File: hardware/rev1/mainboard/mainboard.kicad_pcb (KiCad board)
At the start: 2 copper layers, 40 x 108 mm, 60 parts, among them J1 CONN_05X2SHD, J2 Conn_01x10_Female, J3 Conn_01x10_Female, U1 LM1117-5.0, U2 TPS79633, U3 SAMD51J, U4 OPA388, U5 W25Q32FVSS, U6 AD5685xRUZ, U7 SN74AHCT125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

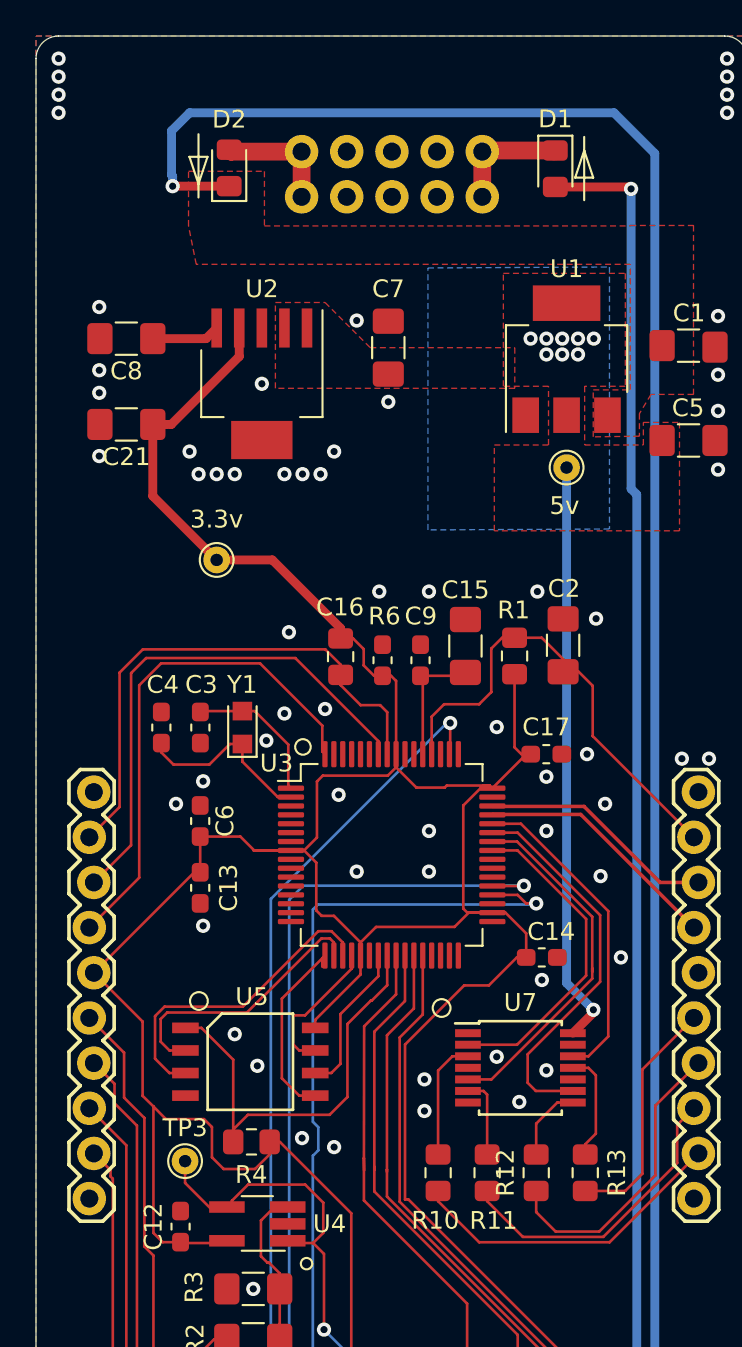
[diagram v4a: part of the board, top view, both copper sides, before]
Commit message: Fix some component sizes
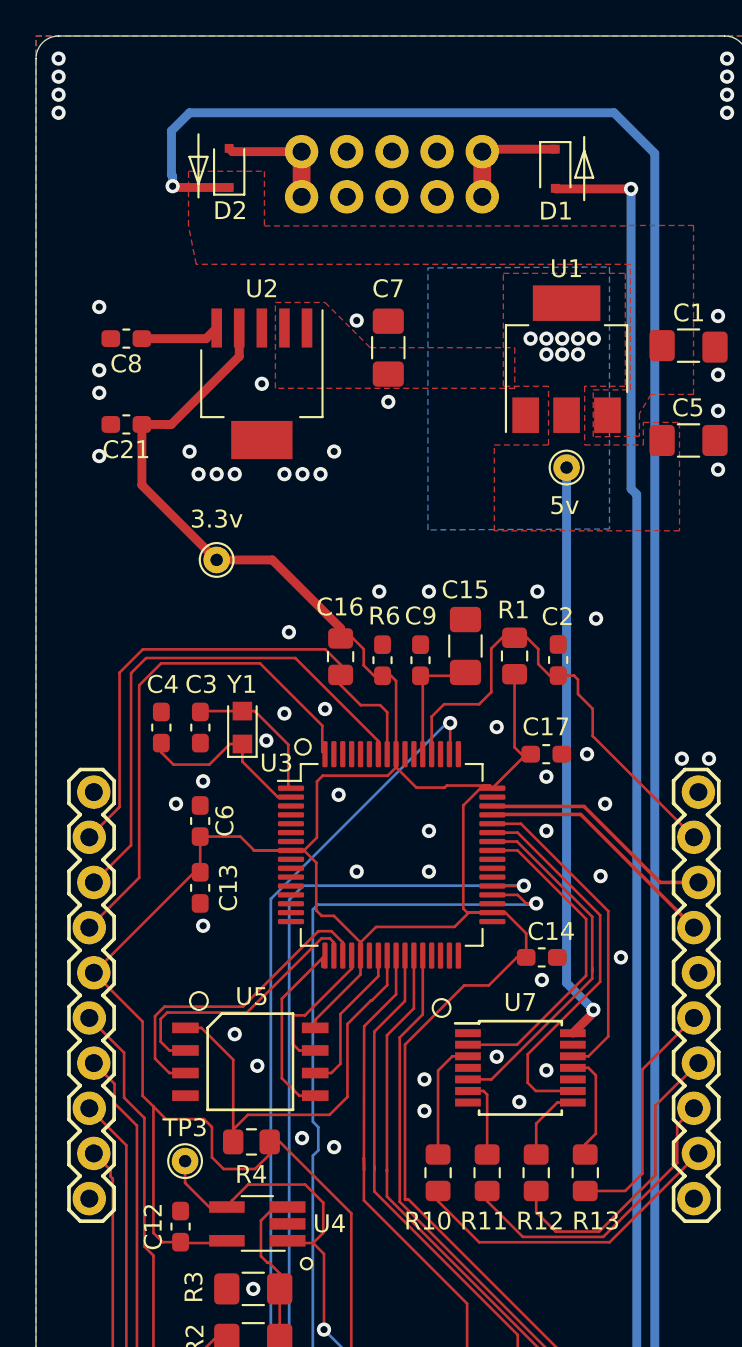
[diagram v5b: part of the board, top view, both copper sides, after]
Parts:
- C2, C21, C8: footprint Capacitor_SMD:C_1206_3216Metric_Pad1.42x1.75mm_HandSolder -> Capacitor_SMD:C_0603_1608Metric_Pad1.05x0.95mm_HandSolder
- D1, D2: value D -> BAS16J,135; footprint Diode_SMD:D_0805_2012Metric_Pad1.15x1.40mm_HandSolder -> Diode_SMD:D_SOD-323F
- moved C2 0.87 mm to (146.4, 85.1)
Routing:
- net VDDIO: track 215.6 -> 216.5 mm
- net Net-(C8-Pad1): track 3.84 -> 4.45 mm

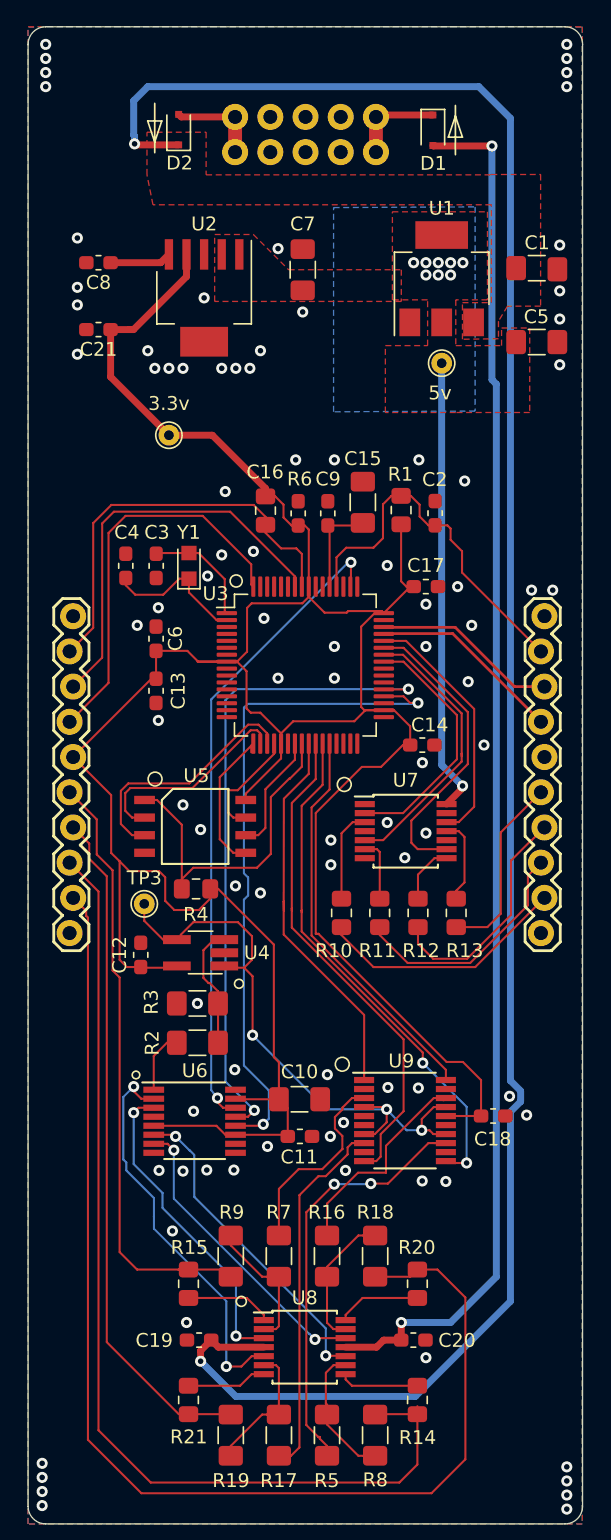
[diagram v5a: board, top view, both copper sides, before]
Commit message: Move to the AD5686R, drop the TMUX
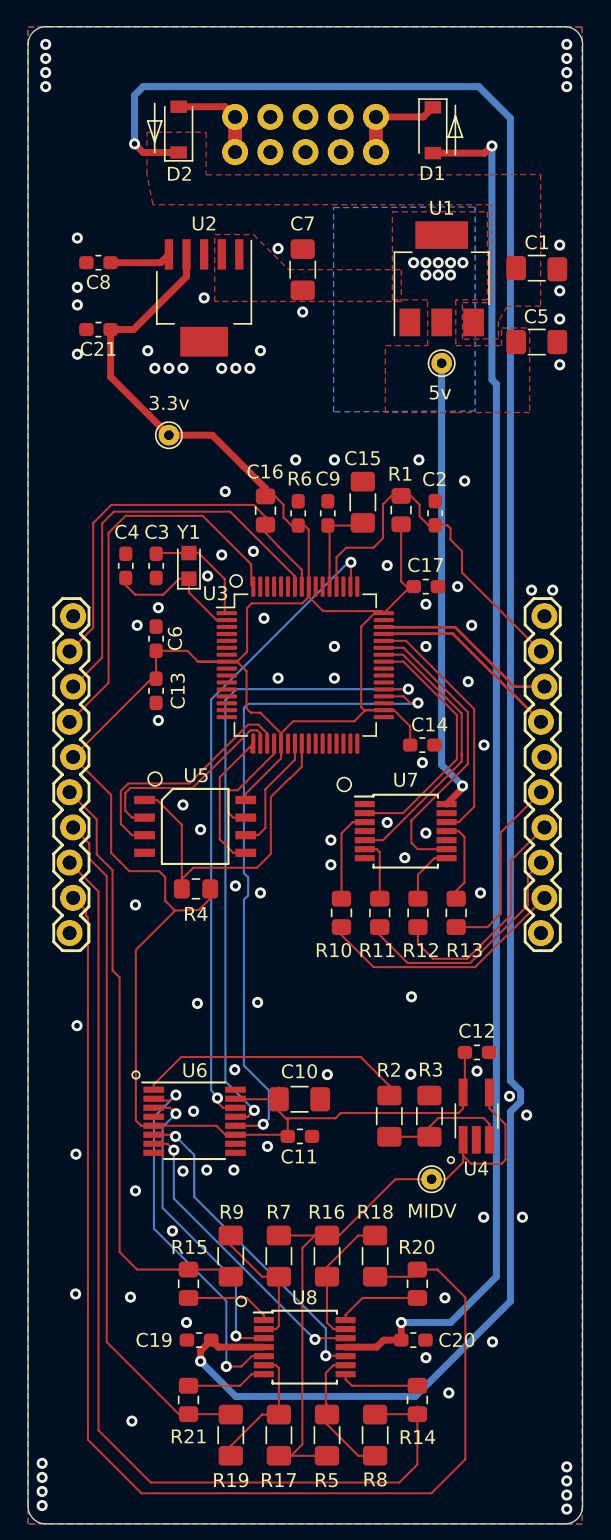
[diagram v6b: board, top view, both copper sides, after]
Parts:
- removed C18: 0.1uF, Capacitor_SMD:C_0603_1608Metric_Pad1.05x0.95mm_HandSolder
- removed U9: TMUX1134, Package_SO:TSSOP-20_4.4x6.5mm_P0.65mm
- added REF**: OSHW-Logo2_7.3x6mm_SilkScreen, Symbol:OSHW-Logo2_7.3x6mm_SilkScreen, B.Cu at (151.5, 154.5)
- D1, D2: value BAS16J,135 -> 1N4148W; footprint Diode_SMD:D_SOD-323F -> Diode_SMD:D_SOD-123
- R16, R17, R5, R7: value 2.94k 0.1% -> 2.15k 0.1%
- R18, R19, R8, R9: value 9.09k 0.1% -> 9.10k 0.1%
- R2: value 4.70k 0.1% -> 1.10k 0.1%
- R3: value 9.09k 0.1% -> 1.00k 0.1%
- U6: value AD5685xRUZ -> AD5686xRUZ
- moved TP3 28.7 mm to (146.1, 133.1)
- moved C12 25.3 mm to (149.4, 124.0), turned to 180 degrees
- moved U4 23.1 mm to (149.3, 128.6), turned to 90 degrees
- moved R3 18.6 mm to (146.0, 128.6), turned to 90 degrees
- moved R2 14.8 mm to (143.1, 128.6), turned to 270 degrees
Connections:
- R16 pad 2: VREF_D -> MIDVREF
- R17 pad 2: VREF_B -> MIDVREF
- R5 pad 2: VREF_C -> MIDVREF
- R7 pad 2: VREF_A -> MIDVREF
- U3 pad 25: RANGE_A -> Net-(U3-Pad25)
- U3 pad 26: RANGE_B -> Net-(U3-Pad26)
- U3 pad 27: RANGE_C -> Net-(U3-Pad27)
- U3 pad 28: RANGE_D -> Net-(U3-Pad28)
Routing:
- net RANGE_C: track 37.5 -> 0.00 mm, vias 2 -> 0
- net RANGE_B: track 36.1 -> 0.00 mm
- net VDDIO: track 216.5 -> 183.9 mm
- net VREF_C: track 31.3 -> 0.00 mm, vias 2 -> 0
- net RANGE_D: track 28.8 -> 0.00 mm
- net RANGE_A: track 28.1 -> 0.00 mm
- net VREF_B: track 27.1 -> 0.00 mm
- net VREF_D: track 15.4 -> 0.00 mm
- net 2V5REF: track 4.50 -> 19.8 mm
- net VREF_A: track 14.4 -> 0.00 mm
- net MIDVREF: track 44.1 -> 47.7 mm, vias 3 -> 0
- net DAC_OUT_B: track 28.6 -> 27.3 mm
- net SWCLK: track 30.1 -> 29.5 mm
- net GND: vias 90 -> 99
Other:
- board text added: "Alethea Flowers CC-BY-SA 4.0 v5 2020/1/15 wntr.dev"
- board text removed: "Alethea Flowers CC-BY-SA 4.0 v4 2020/1/13 wntr.dev"

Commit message: Update some cap sizes
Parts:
- C1, C5, C7: footprint Capacitor_SMD:C_1206_3216Metric_Pad1.42x1.75mm_HandSolder -> Capacitor_SMD:C_0805_2012Metric_Pad1.15x1.40mm_HandSolder
- moved C1 0.41 mm to (154.1, 67.4)
- moved C7 0.30 mm to (136.8, 67.2)
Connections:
- U6 pad 16: GND -> VDDIO

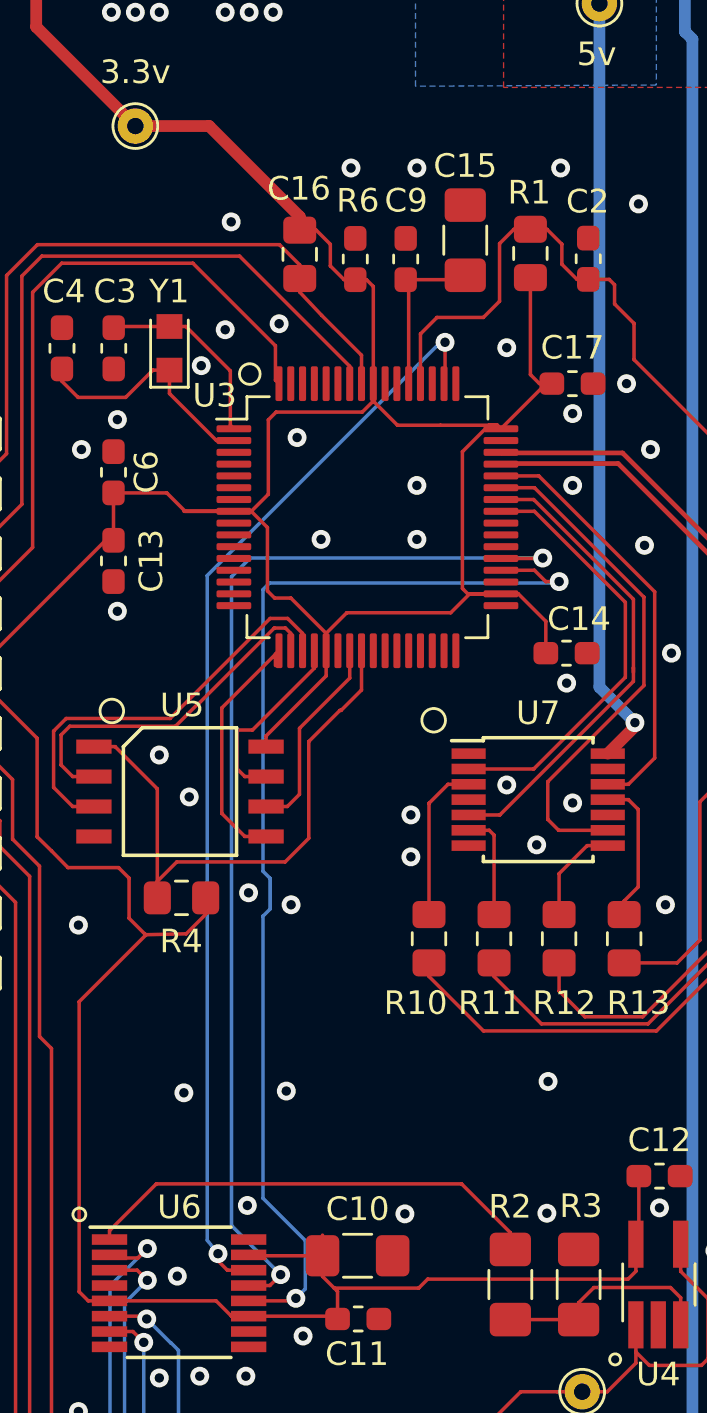
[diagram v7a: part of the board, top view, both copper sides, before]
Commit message: Assign MPNs to all symbols
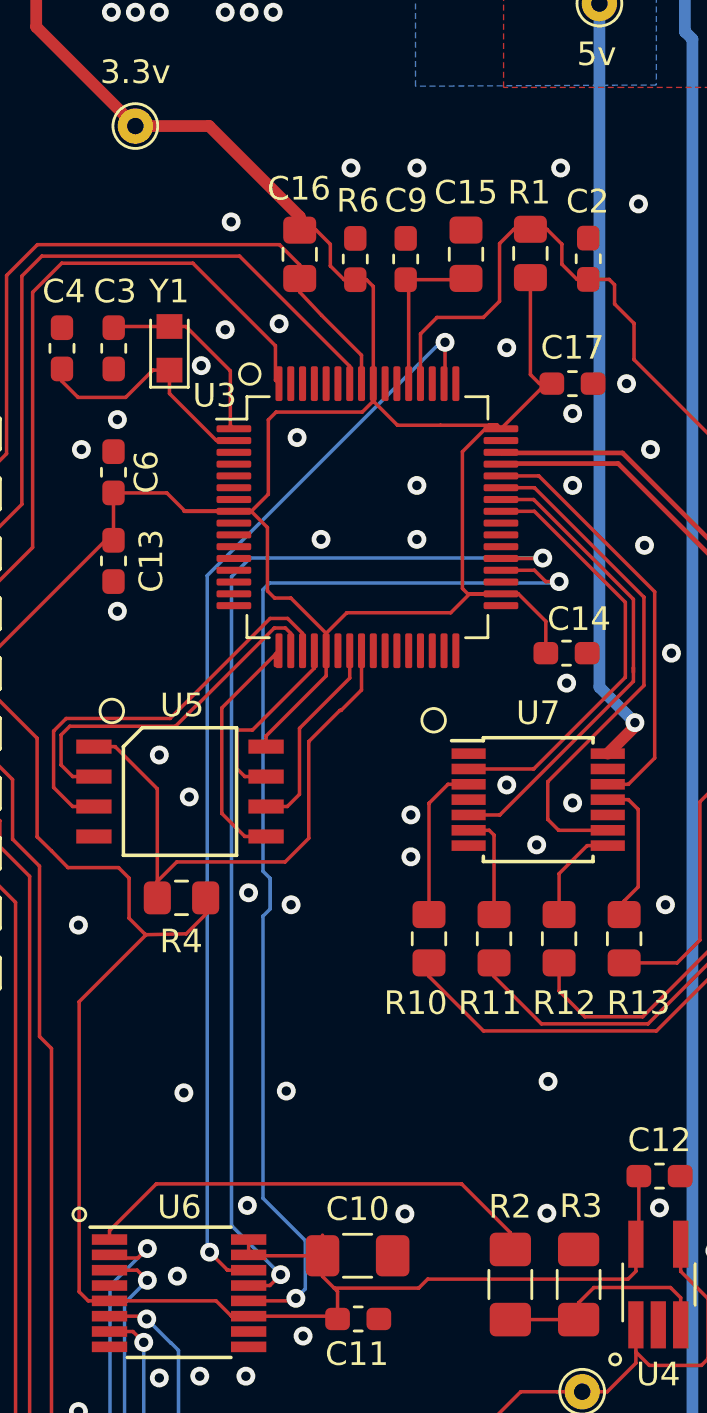
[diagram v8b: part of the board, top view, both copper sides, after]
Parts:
- C15: footprint Capacitor_SMD:C_1206_3216Metric_Pad1.42x1.75mm_HandSolder -> Capacitor_SMD:C_0805_2012Metric_Pad1.15x1.40mm_HandSolder
- moved C15 0.60 mm to (141.2, 84.9)
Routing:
- net VDDIO: track 183.9 -> 184.5 mm
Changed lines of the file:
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@@
     (thickness 1.6)
     (drawings 35)
-    (tracks 636)
+    (tracks 637)
     (zones 0)
     (modules 59)
@@
     )
   )
-  (module Capacitor_SMD:C_1206_3216Metric_Pad1.42x1.75mm_HandSolder (layer F.Cu)
-    (at 141.149 84.3032 90)
-    (descr "Capacitor SMD 1206 (3216 Metric), square (rectangular) end terminal, IPC_7351 nominal with elongated pad for handsoldering. (Body size source: http://www.tortai-tech.com/upload/download/2011102023233369053.pdf), generated with kicad-footprint-generator")
-    (tags "capacitor handsolder")
-    (attr smd)
-    (fp_text reference C15 (at 3.1496 0) (layer F.SilkS)
-      (effects (font (size 1 1) (thickness 0.15)))
-    )
-    (fp_text value 4.7uF (at 0 1.82 90) (layer F.Fab)
-      (effects (font (size 1 1) (thickness 0.15)))
-    )
-    (fp_text user %R (at 0 0 90) (layer F.Fab)
-      (effects (font (size 0.8 0.8) (thickness 0.12)))
-    )
-    (fp_line (start 2.45 1.12) (end -2.45 1.12) (layer F.CrtYd) (width 0.05))
-    (fp_line (start 2.45 -1.12) (end 2.45 1.12) (layer F.CrtYd) (width 0.05))
-    (fp_line (start -2.45 -1.12) (end 2.45 -1.12) (layer F.CrtYd) (width 0.05))
-    (fp_line (start -2.45 1.12) (end -2.45 -1.12) (layer F.CrtYd) (width 0.05))
-    (fp_line (start -0.602064 0.91) (end 0.602064 0.91) (layer F.SilkS) (width 0.12))
-    (fp_line (start -0.602064 -0.91) (end 0.602064 -0.91) (layer F.SilkS) (width 0.12))
-    (fp_line (start 1.6 0.8) (end -1.6 0.8) (layer F.Fab) (width 0.1))
-    (fp_line (start 1.6 -0.8) (end 1.6 0.8) (layer F.Fab) (width 0.1))
-    (fp_line (start -1.6 -0.8) (end 1.6 -0.8) (layer F.Fab) (width 0.1))
-    (fp_line (start -1.6 0.8) (end -1.6 -0.8) (layer F.Fab) (width 0.1))
-    (pad 2 smd roundrect (at 1.4875 0 90) (size 1.425 1.75) (layers F.Cu F.Paste F.Mask) (roundrect_rratio 0.175439)
-      (net 1 GND))
-    (pad 1 smd roundrect (at -1.4875 0 90) (size 1.425 1.75) (layers F.Cu F.Paste F.Mask) (roundrect_rratio 0.175439)
-      (net 62 VDDCORE))
-    (model ${KISYS3DMOD}/Capacitor_SMD.3dshapes/C_1206_3216Metric.wrl
-      (at (xyz 0 0 0))
-      (scale (xyz 1 1 1))
-      (rotate (xyz 0 0 0))
-    )
-  )
   (module Package_QFP:TQFP-64_10x10mm_P0.5mm (layer F.Cu)
     (at 137 96.05)
@@
     )
   )
+  (module Capacitor_SMD:C_0805_2012Metric_Pad1.15x1.40mm_HandSolder (layer F.Cu)
+    (at 141.1808 84.8996 90)
+    (descr "Capacitor SMD 0805 (2012 Metric), square (rectangular) end terminal, IPC_7351 nominal with elongated pad for handsoldering. (Body size source: https://docs.google.com/spreadsheets/d/1BsfQQcO9C6DZCsRaXUlFlo91Tg2WpOkGARC1WS5S8t0/edit?usp=sharing), generated with kicad-footprint-generator")
+    (tags "capacitor handsolder")
+    (attr smd)
+    (fp_text reference C15 (at 2.6162 0 180) (layer F.SilkS)
+      (effects (font (size 1 1) (thickness 0.15)))
+    )
+    (fp_text value 4.7uF (at 0 1.65 90) (layer F.Fab)
+      (effects (font (size 1 1) (thickness 0.15)))
+    )
+    (fp_line (start -1 0.6) (end -1 -0.6) (layer F.Fab) (width 0.1))
+    (fp_line (start -1 -0.6) (end 1 -0.6) (layer F.Fab) (width 0.1))
+    (fp_line (start 1 -0.6) (end 1 0.6) (layer F.Fab) (width 0.1))
+    (fp_line (start 1 0.6) (end -1 0.6) (layer F.Fab) (width 0.1))
+    (fp_line (start -0.261252 -0.71) (end 0.261252 -0.71) (layer F.SilkS) (width 0.12))
+    (fp_line (start -0.261252 0.71) (end 0.261252 0.71) (layer F.SilkS) (width 0.12))
+    (fp_line (start -1.85 0.95) (end -1.85 -0.95) (layer F.CrtYd) (width 0.05))
+    (fp_line (start -1.85 -0.95) (end 1.85 -0.95) (layer F.CrtYd) (width 0.05))
+    (fp_line (start 1.85 -0.95) (end 1.85 0.95) (layer F.CrtYd) (width 0.05))
+    (fp_line (start 1.85 0.95) (end -1.85 0.95) (layer F.CrtYd) (width 0.05))
+    (fp_text user %R (at 0 0 90) (layer F.Fab)
+      (effects (font (size 0.5 0.5) (thickness 0.08)))
+    )
+    (pad 1 smd roundrect (at -1.025 0 90) (size 1.15 1.4) (layers F.Cu F.Paste F.Mask) (roundrect_rratio 0.217391)
+      (net 62 VDDCORE))
+    (pad 2 smd roundrect (at 1.025 0 90) (size 1.15 1.4) (layers F.Cu F.Paste F.Mask) (roundrect_rratio 0.217391)
+      (net 1 GND))
+    (model ${KISYS3DMOD}/Capacitor_SMD.3dshapes/C_0805_2012Metric.wrl
+      (at (xyz 0 0 0))
+      (scale (xyz 1 1 1))
+      (rotate (xyz 0 0 0))
+    )
+  )
   (gr_circle (center 147.5054 131.7626) (end 147.734 131.8134) (layer F.SilkS) (width 0.12))
   (gr_line (start 137 50) (end 137 157) (layer Dwgs.User) (width 0.15))
@@
   (segment (start 138.275 92.15) (end 137.25 91.125) (width 0.15) (layer F.Cu) (net 6))
   (segment (start 140.1 92.15) (end 138.275 92.15) (width 0.15) (layer F.Cu) (net 6))
+  (segment (start 131.9642 127.3301) (end 131.9642 126.6801) (width 0.15) (layer F.Cu) (net 6))
   (segment (start 131.9352 59.0424) (end 131.9352 56.5024) (width 1) (layer F.Cu) (net 7) (status 30))
   (segment (start 131.2016 55.7688) (end 131.9352 56.5024) (width 0.5) (layer F.Cu) (net 7))
@@
   (segment (start 149.1818 106.261) (end 148.0665 107.3763) (width 0.15) (layer F.Cu) (net 50))
   (segment (start 142.6625 94.3) (end 144.2693 94.3) (width 0.15) (layer F.Cu) (net 50) (status 10))
-  (segment (start 131.0642 127.9801) (end 130.664198 127.580098) (width 0.15) (layer F.Cu) (net 51))
-  (via (at 130.664198 127.2795) (size 0.8) (drill 0.4) (layers F.Cu B.Cu) (net 51))
-  (segment (start 130.664198 127.580098) (end 130.664198 127.2795) (width 0.15) (layer F.Cu) (net 51))
+  (via (at 130.3096 127.216) (size 0.8) (drill 0.4) (layers F.Cu B.Cu) (net 51))
   (segment (start 131.9642 127.9801) (end 131.0642 127.9801) (width 0.15) (layer F.Cu) (net 51) (status 10))
   (via (at 140.2918 88.6334) (size 0.8) (drill 0.4) (layers F.Cu B.Cu) (net 51))
   (segment (start 140.2918 90.3457) (end 140.25 90.3875) (width 0.15) (layer F.Cu) (net 51) (status 30))
   (segment (start 140.2918 88.6334) (end 140.2918 90.3457) (width 0.15) (layer F.Cu) (net 51) (status 20))
-  (segment (start 140.1013 88.6334) (end 140.2918 88.6334) (width 0.15) (layer B.Cu) (net 51))
-  (segment (start 130.208 98.5267) (end 140.1013 88.6334) (width 0.15) (layer B.Cu) (net 51))
-  (segment (start 130.208 126.708) (end 130.208 98.5267) (width 0.15) (layer B.Cu) (net 51))
-  (segment (start 130.664198 127.2795) (end 130.208 126.708) (width 0.15) (layer B.Cu) (net 51))
+  (segment (start 131.0642 127.9706) (end 130.3096 127.216) (width 0.15) (layer F.Cu) (net 51))
+  (segment (start 131.0642 127.9801) (end 131.0642 127.9706) (width 0.15) (layer F.Cu) (net 51))
+  (segment (start 130.208 98.5267) (end 130.208 127.1144) (width 0.15) (layer B.Cu) (net 51))
+  (segment (start 140.1013 88.6334) (end 130.208 98.5267) (width 0.15) (layer B.Cu) (net 51))
+  (segment (start 130.208 127.1144) (end 130.3096 127.216) (width 0.15) (layer B.Cu) (net 51))
+  (segment (start 140.2918 88.6334) (end 140.1013 88.6334) (width 0.15) (layer B.Cu) (net 51))
   (segment (start 126.0805 135.8012) (end 126.0805 135.852) (width 0.15) (layer B.Cu) (net 57))
   (via (at 131.3002 146.647) (size 0.8) (drill 0.4) (layers F.Cu B.Cu) (net 57))
